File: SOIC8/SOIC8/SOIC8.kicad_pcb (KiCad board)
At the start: 2 copper layers, 10.7 x 10.7 mm, 5 parts, among them J1 Conn_01x04, J2 Conn_01x04

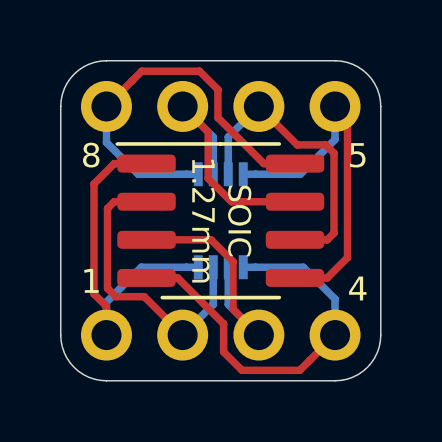
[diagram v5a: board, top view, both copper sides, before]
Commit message: Silkscreen Edits
Dimensions moved to Drawings Layer
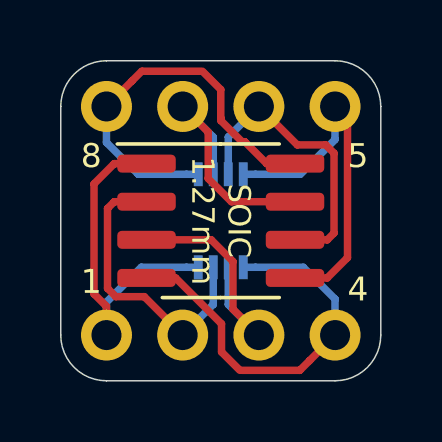
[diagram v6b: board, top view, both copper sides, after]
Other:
- rule pad_to_mask_clearance: 0.051 -> 0
- rule solder_mask_min_width: 0.25 -> 0.1
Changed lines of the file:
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@@
     (thickness 1.6)
     (drawings 22)
-    (tracks 67)
+    (tracks 70)
     (zones 0)
     (modules 5)
@@
     (pad_size 1.7 1.7)
     (pad_drill 1)
-    (pad_to_mask_clearance 0.051)
-    (solder_mask_min_width 0.25)
+    (pad_to_mask_clearance 0)
+    (solder_mask_min_width 0.1)
     (aux_axis_origin 0 0)
     (visible_elements 7FFFFFFF)
@@
       (usegerberadvancedattributes false)
       (creategerberjobfile false)
-      (excludeedgelayer false)
+      (excludeedgelayer true)
       (linewidth 0.100000)
       (plotframeref false)
       (viasonmask false)
       (mode 1)
-      (useauxorigin false)
+      (useauxorigin true)
       (hpglpennumber 1)
       (hpglpenspeed 20)
@@
     (effects (font (size 0.8 0.8) (thickness 0.13)))
   )
-  (dimension 7.62 (width 0.15) (layer F.SilkS)
-    (gr_text "7.620 mm" (at 187.198 95.534) (layer F.SilkS)
+  (dimension 7.62 (width 0.15) (layer Dwgs.User)
+    (gr_text "7.620 mm" (at 187.198 95.534) (layer Dwgs.User)
       (effects (font (size 1 1) (thickness 0.15)) hide)
     )
@@
     (arrow2b (pts (xy 191.008 94.234) (xy 189.881496 94.820421)))
   )
-  (dimension 7.62 (width 0.15) (layer F.SilkS)
-    (gr_text "7.620 mm" (at 195.102 87.376 90) (layer F.SilkS)
+  (dimension 7.62 (width 0.15) (layer Dwgs.User)
+    (gr_text "7.620 mm" (at 195.102 87.376 90) (layer Dwgs.User)
       (effects (font (size 1 1) (thickness 0.15)) hide)
     )
@@
     (arrow2b (pts (xy 193.802 83.566) (xy 194.388421 84.692504)))
   )
-  (dimension 10.668 (width 0.15) (layer F.SilkS)
-    (gr_text "10.668 mm" (at 187.198 98.328) (layer F.SilkS)
+  (dimension 10.668 (width 0.15) (layer Dwgs.User)
+    (gr_text "10.668 mm" (at 187.198 98.328) (layer Dwgs.User)
       (effects (font (size 1 1) (thickness 0.15)) hide)
     )
@@
     (arrow2b (pts (xy 192.532 97.028) (xy 191.405496 97.614421)))
   )
-  (dimension 10.668 (width 0.15) (layer F.SilkS)
-    (gr_text "10.668 mm" (at 197.769 87.376 90) (layer F.SilkS)
+  (dimension 10.668 (width 0.15) (layer Dwgs.User)
+    (gr_text "10.668 mm" (at 197.769 87.376 90) (layer Dwgs.User)
       (effects (font (size 1 1) (thickness 0.15)) hide)
     )
@@
   (segment (start 184.237999 82.716001) (end 183.388 83.566) (width 0.25) (layer F.Cu) (net 4))
   (segment (start 184.563001 82.390999) (end 184.237999 82.716001) (width 0.25) (layer F.Cu) (net 4))
-  (segment (start 186.492001 82.390999) (end 184.563001 82.390999) (width 0.25) (layer F.Cu) (net 4))
-  (segment (start 187.103001 83.001999) (end 186.492001 82.390999) (width 0.25) (layer F.Cu) (net 4))
-  (segment (start 187.103001 83.940003) (end 187.103001 83.001999) (width 0.25) (layer F.Cu) (net 4))
-  (segment (start 188.633998 85.471) (end 187.103001 83.940003) (width 0.25) (layer F.Cu) (net 4))
-  (segment (start 189.773 85.471) (end 188.633998 85.471) (width 0.25) (layer F.Cu) (net 4))
+  (segment (start 186.5122 82.390999) (end 184.5832 82.390999) (width 0.25) (layer F.Cu) (net 4))
+  (segment (start 187.198 83.001999) (end 186.587 82.390999) (width 0.25) (layer F.Cu) (net 4))
   (segment (start 186.048 85.826) (end 186.448 85.826) (width 0.25) (layer B.Cu) (net 4))
   (segment (start 184.445919 85.826) (end 186.048 85.826) (width 0.25) (layer B.Cu) (net 4))
   (segment (start 183.388 84.768081) (end 184.445919 85.826) (width 0.25) (layer B.Cu) (net 4))
   (segment (start 183.388 83.566) (end 183.388 84.768081) (width 0.25) (layer B.Cu) (net 4))
+  (segment (start 187.198 83.940003) (end 187.198 83.001999) (width 0.25) (layer F.Cu) (net 4))
+  (segment (start 187.198 84.035002) (end 187.198 83.940003) (width 0.25) (layer F.Cu) (net 4))
+  (segment (start 187.903999 84.741001) (end 187.198 84.035002) (width 0.25) (layer F.Cu) (net 4))
+  (segment (start 187.998998 84.741001) (end 187.903999 84.741001) (width 0.25) (layer F.Cu) (net 4))
+  (segment (start 189.773 85.471) (end 188.728997 85.471) (width 0.25) (layer F.Cu) (net 4))
+  (segment (start 188.728997 85.471) (end 187.998998 84.741001) (width 0.25) (layer F.Cu) (net 4))
   (segment (start 189.950081 88.926) (end 188.348 88.926) (width 0.25) (layer B.Cu) (net 5))
   (segment (start 188.348 88.926) (end 187.948 88.926) (width 0.25) (layer B.Cu) (net 5))
@@
   (segment (start 189.832999 92.361001) (end 190.158001 92.035999) (width 0.25) (layer F.Cu) (net 5))
   (segment (start 187.903999 92.361001) (end 189.832999 92.361001) (width 0.25) (layer F.Cu) (net 5))
-  (segment (start 187.292999 91.750001) (end 187.903999 92.361001) (width 0.25) (layer F.Cu) (net 5))
-  (segment (start 187.292999 90.811997) (end 187.292999 91.750001) (width 0.25) (layer F.Cu) (net 5))
-  (segment (start 185.762002 89.281) (end 187.292999 90.811997) (width 0.25) (layer F.Cu) (net 5))
-  (segment (start 184.623 89.281) (end 185.762002 89.281) (width 0.25) (layer F.Cu) (net 5))
+  (segment (start 187.2234 91.750001) (end 187.8344 92.361001) (width 0.25) (layer F.Cu) (net 5))
+  (segment (start 187.2234 90.811997) (end 187.2234 91.750001) (width 0.25) (layer F.Cu) (net 5))
+  (segment (start 185.692403 89.281) (end 187.2234 90.811997) (width 0.25) (layer F.Cu) (net 5))
+  (segment (start 184.623 89.281) (end 185.692403 89.281) (width 0.25) (layer F.Cu) (net 5))
   (segment (start 184.623 88.011) (end 186.8805 88.011) (width 0.25) (layer F.Cu) (net 6))
   (segment (start 186.8805 88.011) (end 187.6044 88.7349) (width 0.25) (layer F.Cu) (net 6))

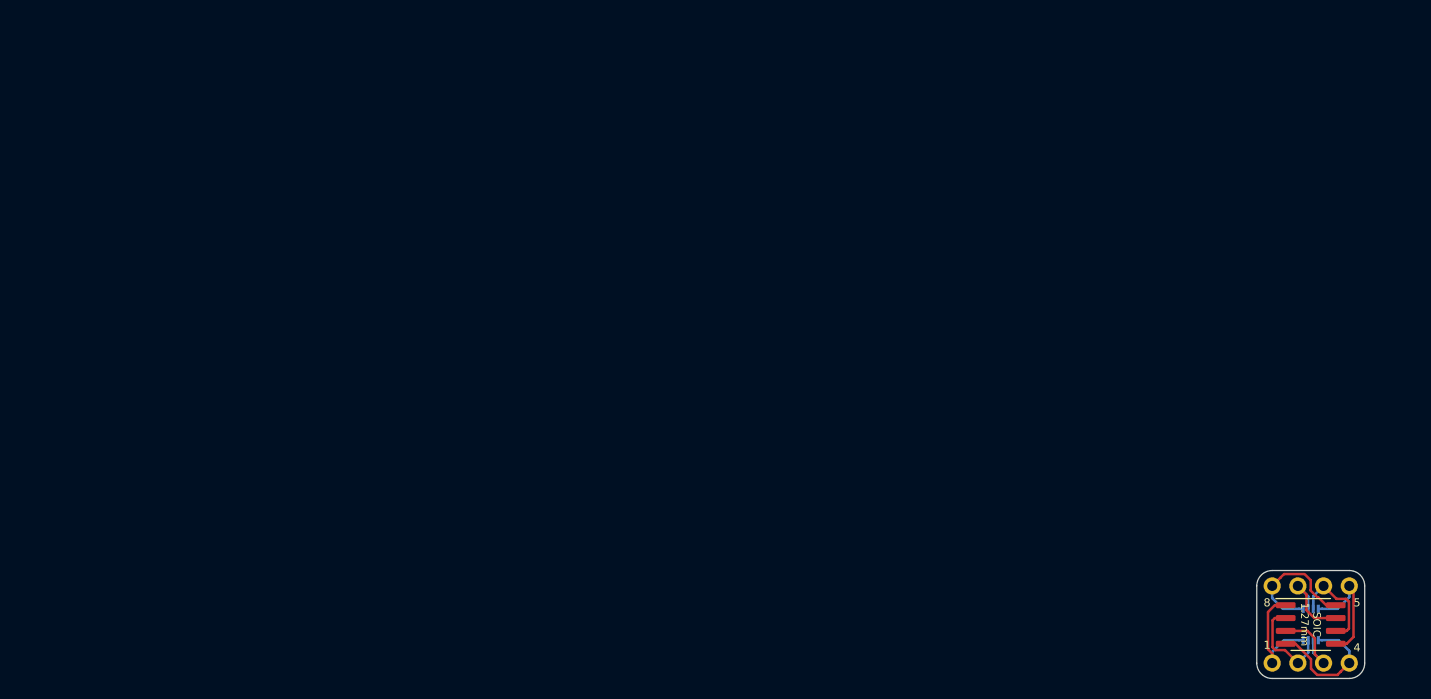
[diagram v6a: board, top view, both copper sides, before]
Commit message: USB, SD and CR Cells Added
MicroSD, MicroUSB, MiniUSB, USB-C, CR1220, CR2032 added as well as all schematics page sizes optimised
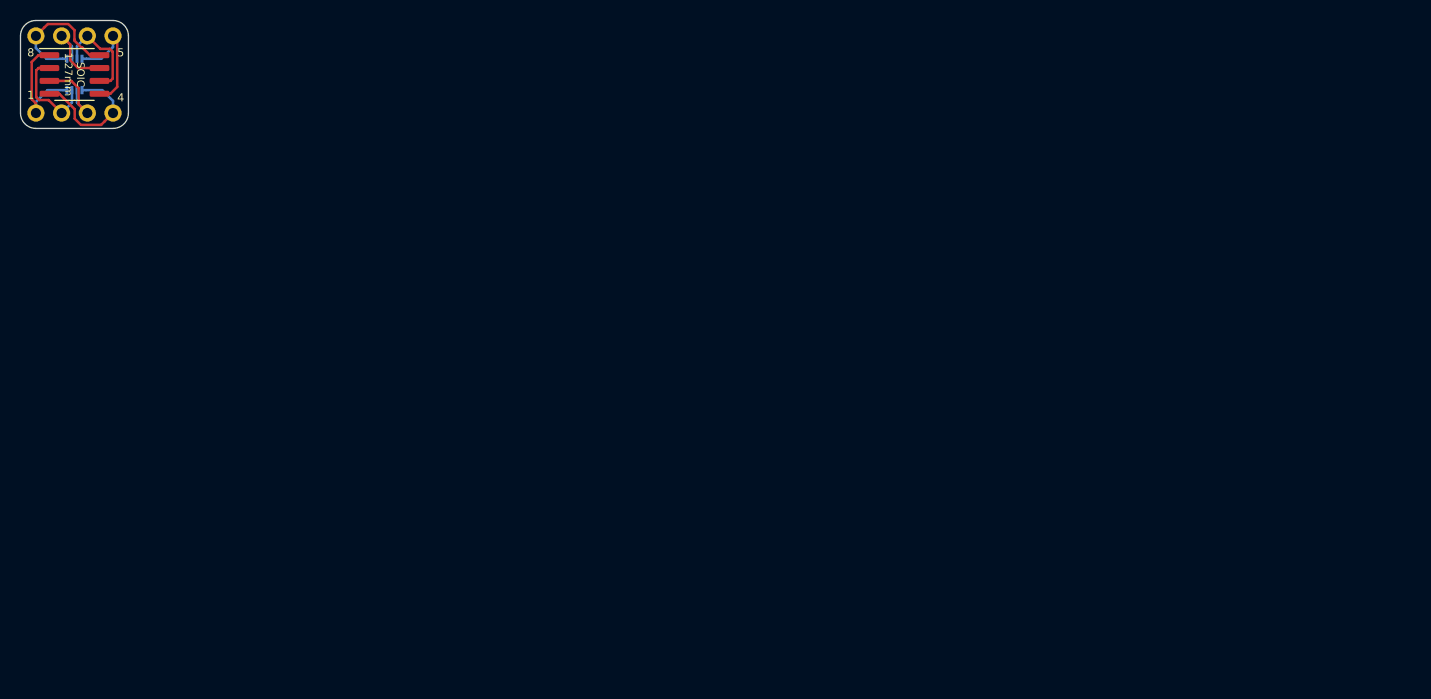
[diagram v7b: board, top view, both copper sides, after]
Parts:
- moved J1 133.7 mm to (61.2, 29.2)
- moved J2 133.7 mm to (61.2, 36.8)
- moved REF** 133.7 mm to (65.0, 33.0)
- moved SOIC/SOIJ 133.7 mm to (65.0, 33.0)
- moved G*** 133.7 mm to (62.1, 33.0)

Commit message: Board Updates
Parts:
- removed REF**: VSSOP-8_2.3x2mm_P0.5mm, Package_SO:VSSOP-8_2.3x2mm_P0.5mm
- removed SOIC/SOIJ: ATtiny85-20SU, Package_SO:SOIC-8_3.9x4.9mm_P1.27mm
- added J3: SOIC8, Package_SO:SOIC-8_3.9x4.9mm_P1.27mm, F.Cu at (65.0, 33.0)
- added J4: VSSOP8, Package_SO:VSSOP-8_2.3x2mm_P0.5mm, B.Cu at (65.1, 32.6)
- moved G*** 3.45 mm to (65.0, 34.9), turned to 0 degrees
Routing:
- net Net-(J1-Pad1): track 13.4 -> 8.07 mm, vias 0 -> 1
- net Net-(J2-Pad4): track 13.3 -> 8.80 mm, vias 0 -> 1
- net Net-(J1-Pad4): track 11.8 -> 9.92 mm, vias 0 -> 1
- net Net-(J2-Pad1): track 11.8 -> 10.3 mm, vias 0 -> 1
- net Net-(J1-Pad3): track 9.79 -> 8.28 mm, vias 0 -> 1
- net Net-(J1-Pad2): track 8.75 -> 7.33 mm, vias 0 -> 1
- net Net-(J2-Pad3): track 8.77 -> 7.57 mm, vias 0 -> 1
- net Net-(J2-Pad2): track 9.79 -> 8.90 mm, vias 0 -> 1
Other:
- board size 10.7 x 10.7 mm -> 10.2 x 10.2 mm
- net class Default: clearance 0.2 -> 0.127; trace_width 0.25 -> 0.127; via_dia 0.8 -> 0.6; via_drill 0.4 -> 0.3
- rule trace_clearance: 0.2 -> 0.127
- rule trace_min: 0.2 -> 0.127
- board text added: "P=0.5mm"
- board text removed: "VSSOP 0.5mm"
